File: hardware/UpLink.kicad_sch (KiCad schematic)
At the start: 20 parts, among them U1 SAM-M10Q-00B, U2 XIAO-ESP32-S3-SMD, U3 114993390, U4 TPS631000DRLR

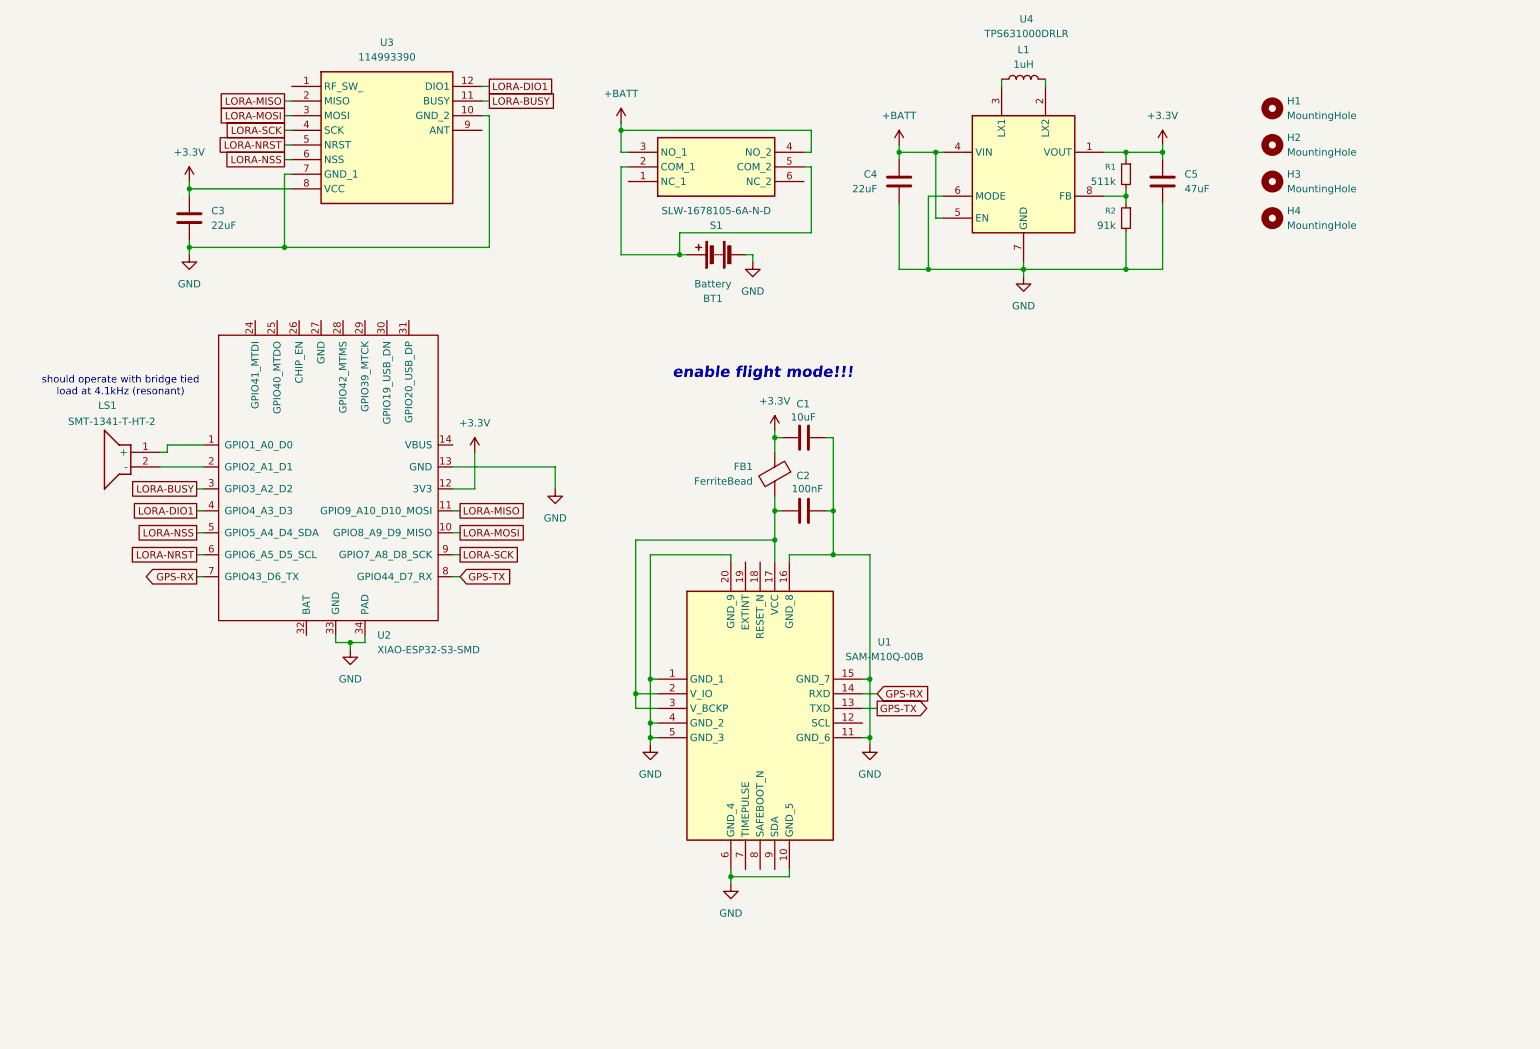
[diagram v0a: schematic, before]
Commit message: Clean up schematic
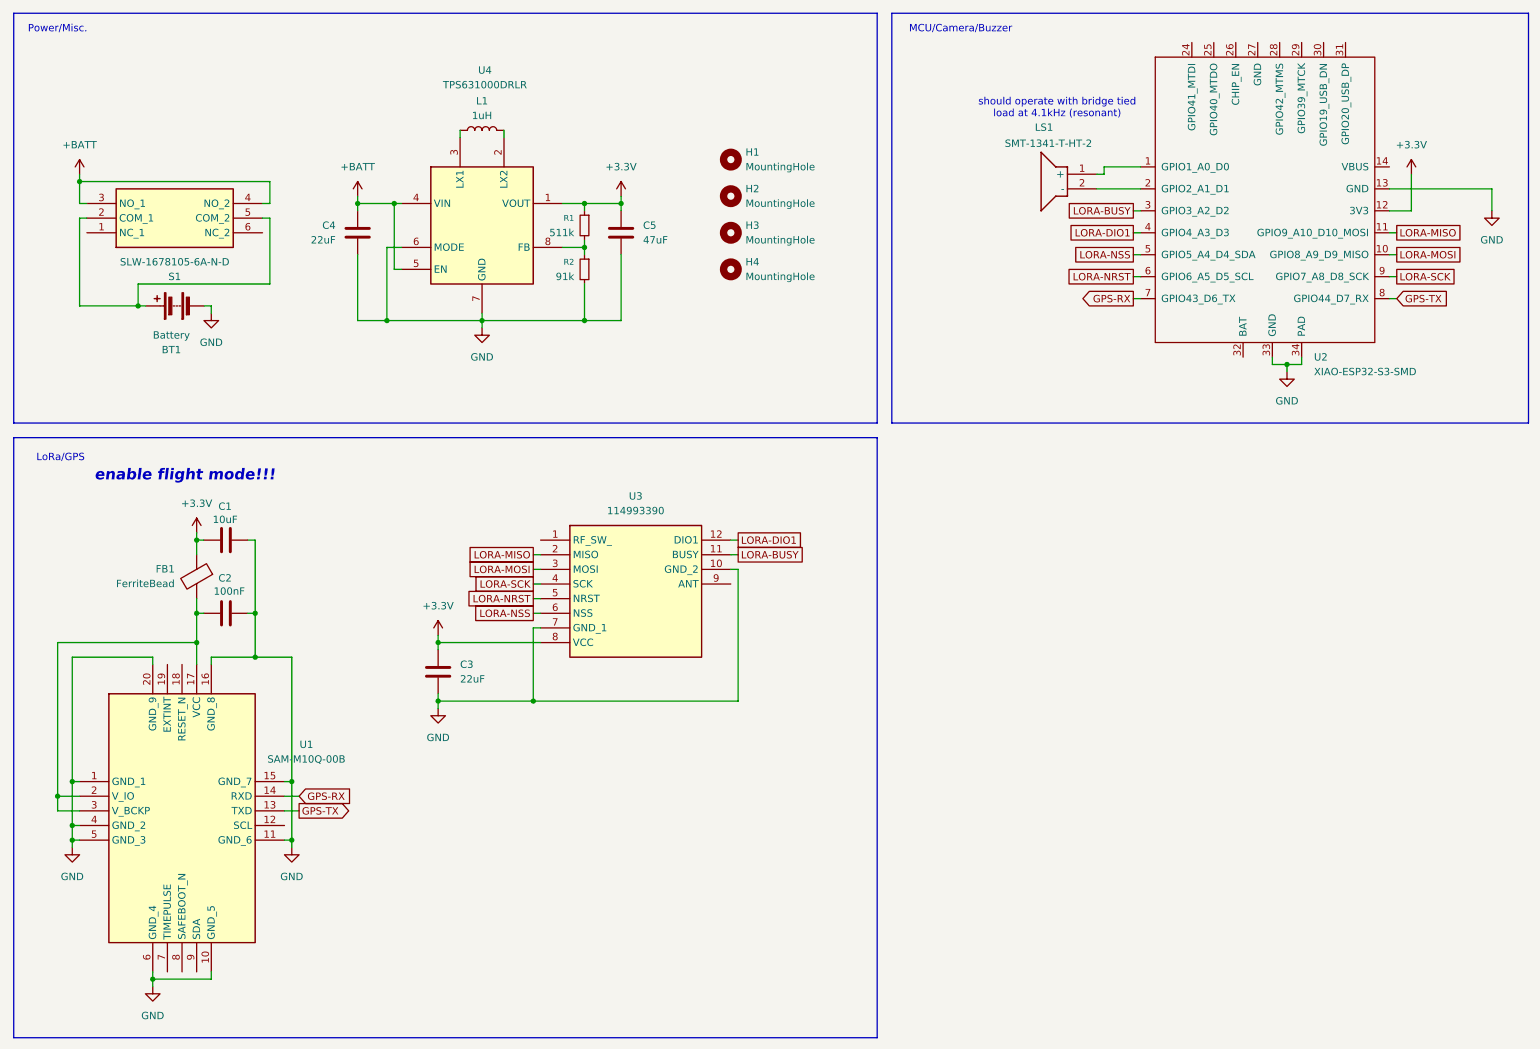
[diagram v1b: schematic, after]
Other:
- note added: "LoRa/GPS"
- note added: "MCU/Camera/Buzzer"
- note added: "Power/Misc."
- moved on the sheet: BT1, C1, C2, C3, C4, C5, FB1, H1, H2, H3, H4, L1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

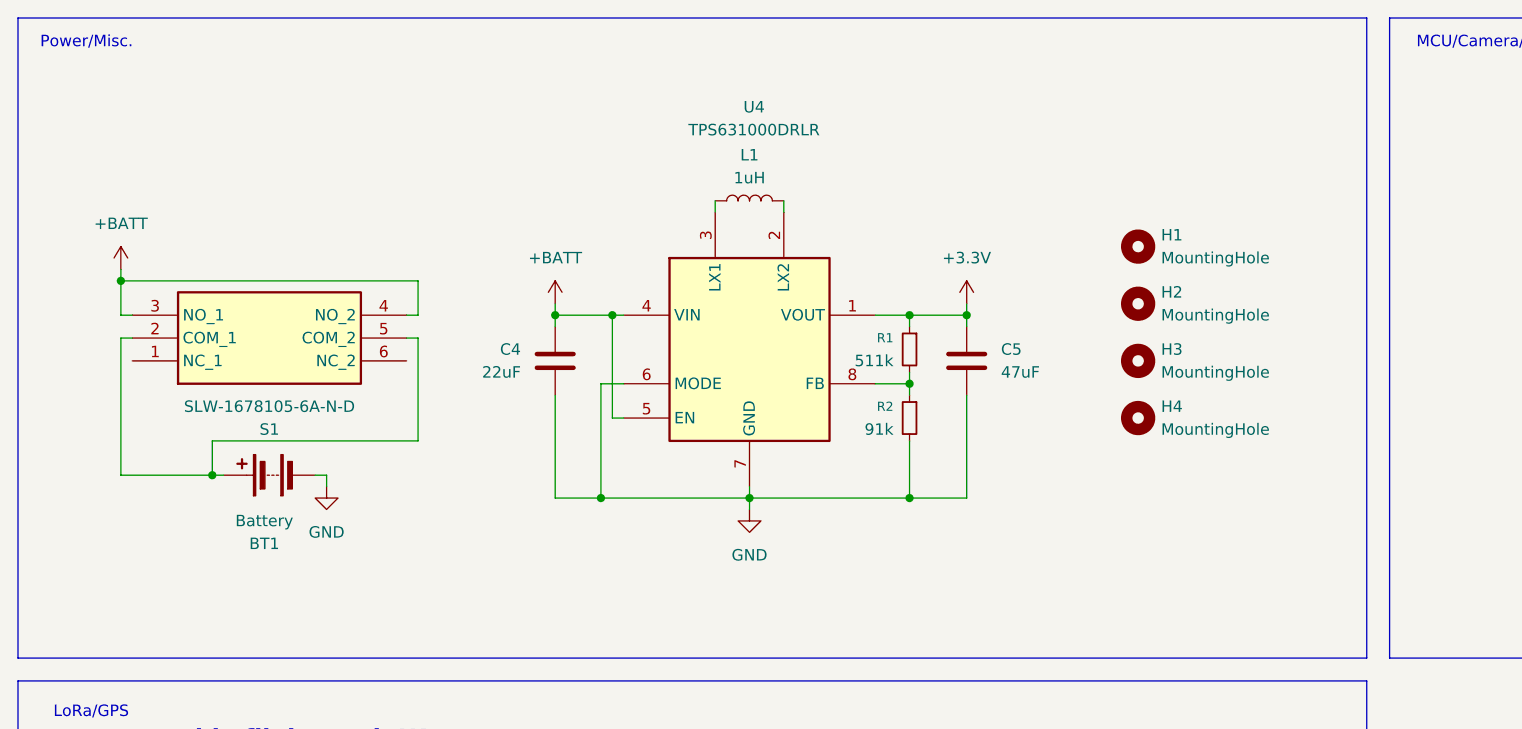
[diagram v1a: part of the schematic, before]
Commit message: Add TPS22917DBV for high side switching of payload, redesign layout for thinner board at cost of slight GPS performance hits
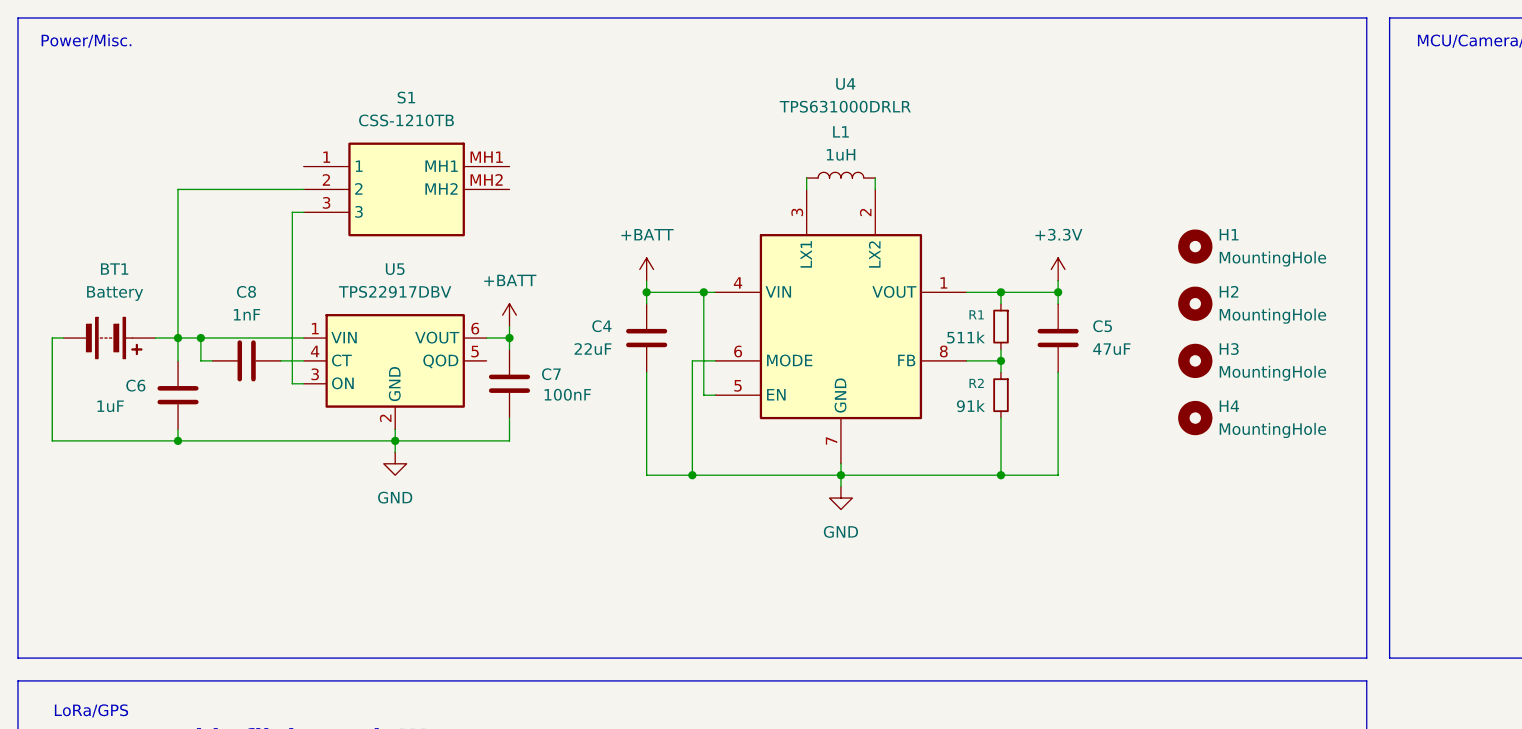
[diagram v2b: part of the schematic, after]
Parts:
- removed S1: SLW-1678105-6A-N-D, SLW-1678105-6A-N-D:SLW16781056AND, symbol SLW-1678105-6A-N-D:SLW-1678105-6A-N-D
- added C6: 1uF, Capacitor_SMD:C_0603_1608Metric, symbol Device:C
- added C7: 100nF, Capacitor_SMD:C_0603_1608Metric, symbol Device:C
- added C8: 1nF, symbol Device:C
- added S1: CSS-1210TB, CSS1210TB, symbol CSS-1210TB:CSS-1210TB
- added U5: TPS22917DBV, Package_TO_SOT_SMD:SOT-23-6, symbol Power_Management:TPS22917DBV
- BT1: Mouser Part (none) -> 12BHC431A-GR
- H1, H2, H3, H4: footprint MountingHole:MountingHole_2.2mm_M2 -> MountingHole:MountingHole_2.2mm_M2_Pad
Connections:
- net +BATT: now also C7.2, U5.6 (VOUT)
- net GND: now also C6.1, C7.1, U5.2 (GND)
- net at BT1.1 (+): now also C6.2, C8.1, S1.2, U5.1 (VIN)
- new net: C8.2, U5.4 (CT)
- new net: S1.3, U5.3 (ON)
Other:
- moved on the sheet: BT1, C4, C5, H1, H2, H3, H4, L1, R1, R2, U4

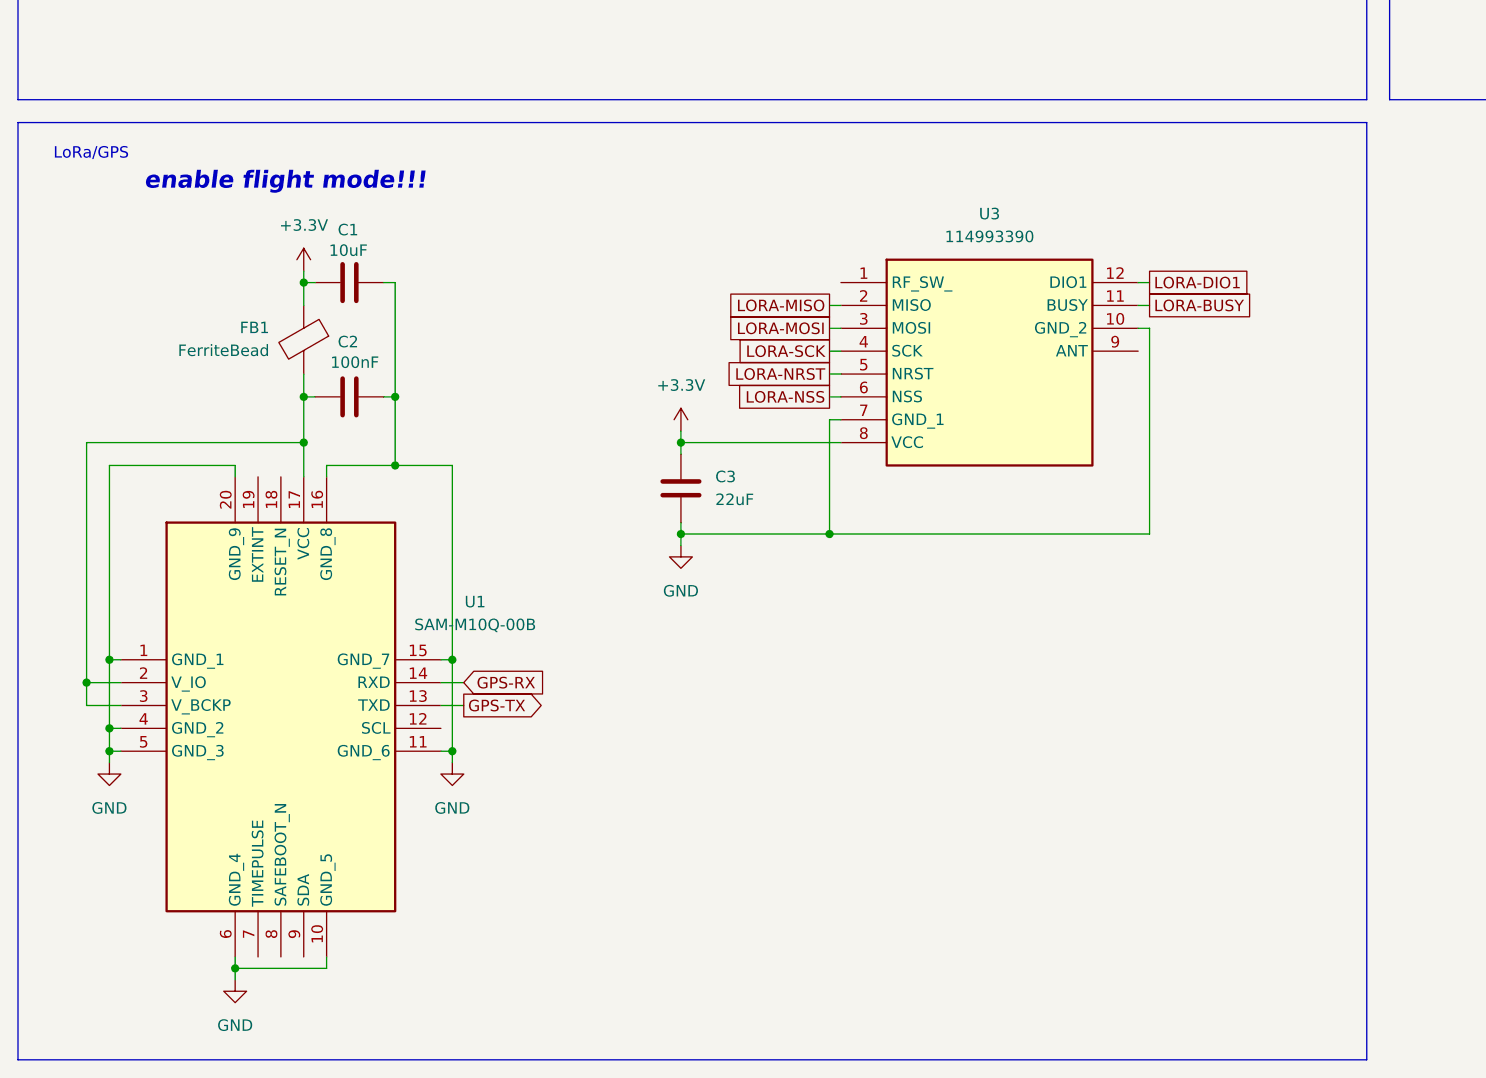
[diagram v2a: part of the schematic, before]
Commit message: Add notes to schematic
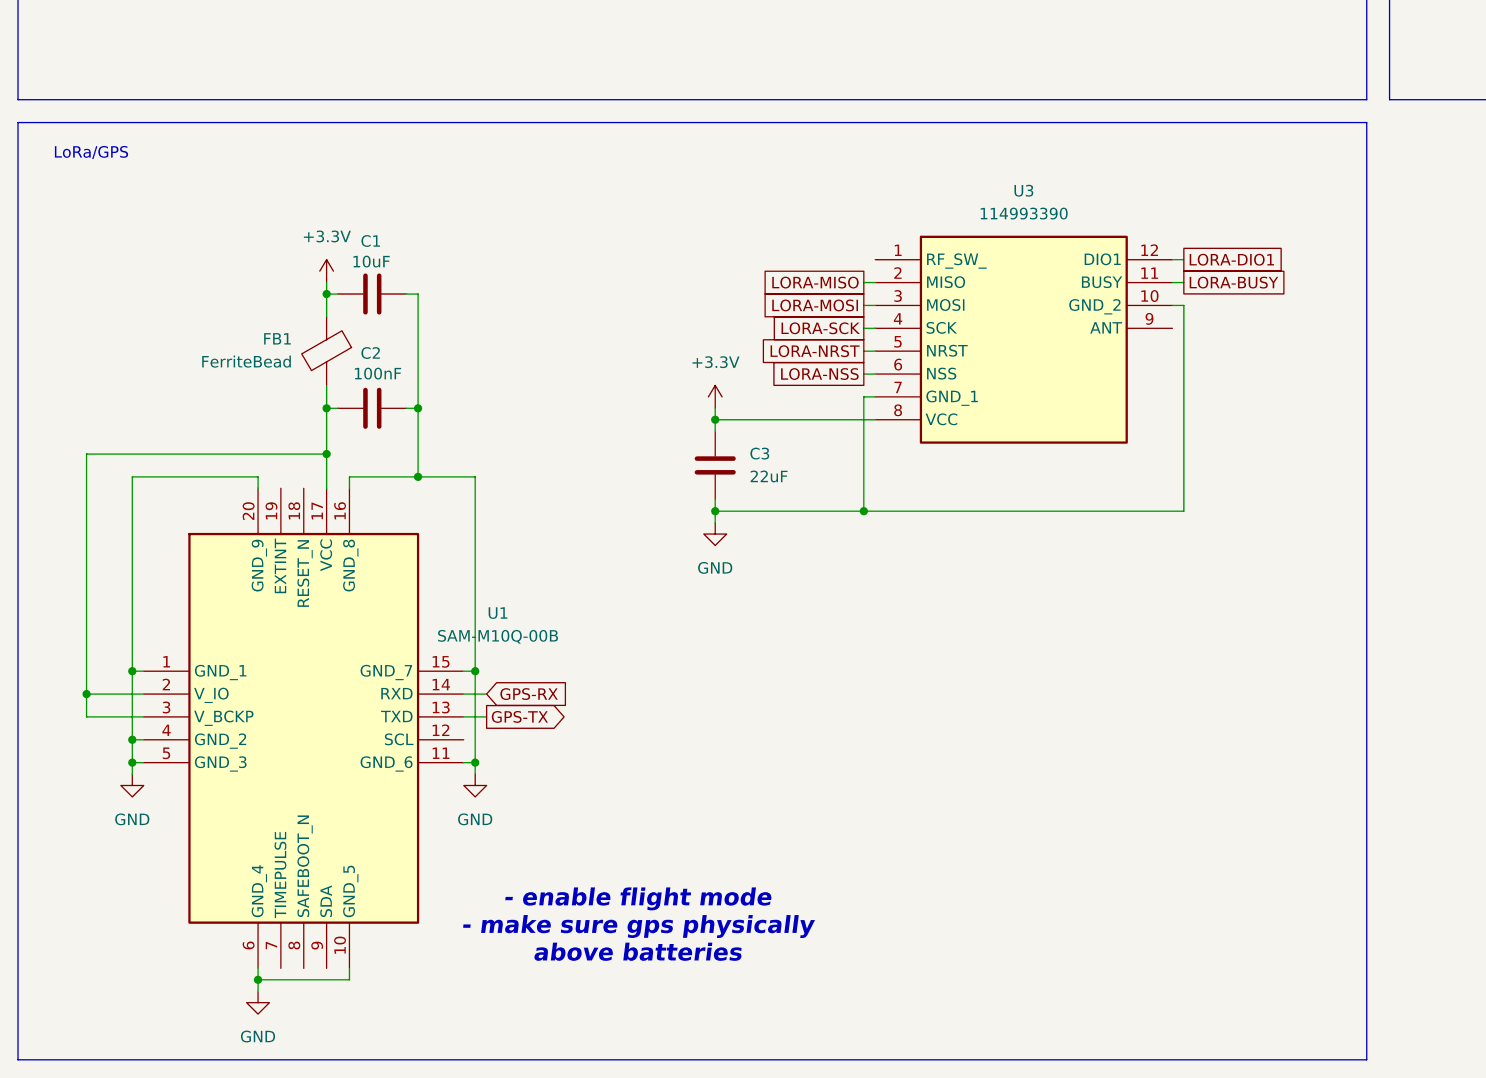
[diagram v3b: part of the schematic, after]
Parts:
- L1: Mouser Part (none) -> 81-DFE252012F-1R0MP2
- R1: Mouser Part (none) -> 603-RT0603FRE07511KL
- R2: Mouser Part (none) -> 603-AC0603JR-0791KL
- U4: Mouser Part (none) -> 595-TPS631000DRLR
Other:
- note added: "- enable flight mode - make sure gps physically above batteries"
- note removed: "enable flight mode!!!"
- moved on the sheet: C1, C2, C3, FB1, U1, U3

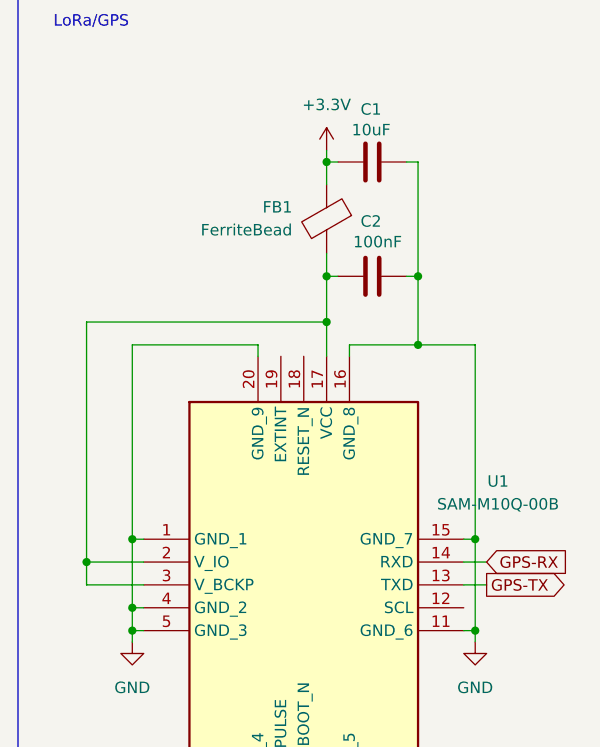
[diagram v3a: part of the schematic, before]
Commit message: Redo layout and routing, space traces apart
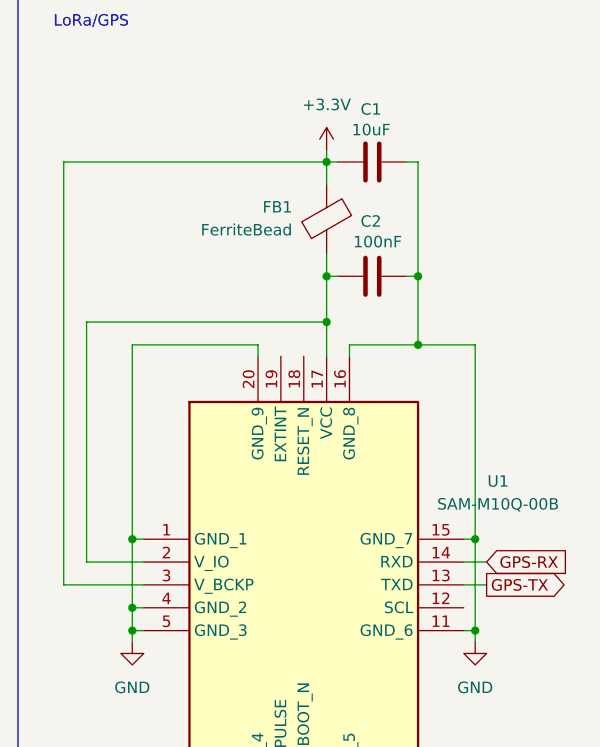
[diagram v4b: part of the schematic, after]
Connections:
- net +3.3V: now also U1.3 (V_BCKP)
- net at C2.1, FB1.2, U1.17 (VCC)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: no longer U1.3 (V_BCKP)
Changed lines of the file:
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@@
-	)
-	(junction
-		(at 26.67 154.94)
-		(diameter 0)
-		(color 0 0 0 0)
 	)
 	(junction
@@
 	(wire
 		(pts
-			(xy 26.67 154.94) (xy 26.67 157.48)
-		)
-		(stroke
-			(width 0)
-			(type default)
-		)
-	)
-	(wire
-		(pts
 			(xy 208.28 44.45) (xy 214.63 44.45)
 		)
@@
 	(wire
 		(pts
+			(xy 33.02 157.48) (xy 24.13 157.48)
+		)
+		(stroke
+			(width 0)
+			(type default)
+		)
+	)
+	(wire
+		(pts
 			(xy 93.98 55.88) (xy 93.98 68.58)
 		)
@@
 	(wire
 		(pts
-			(xy 26.67 157.48) (xy 33.02 157.48)
-		)
-		(stroke
-			(width 0)
-			(type default)
-		)
-	)
-	(wire
-		(pts
 			(xy 93.98 68.58) (xy 110.49 68.58)
 		)
@@
 	(wire
 		(pts
+			(xy 24.13 110.49) (xy 53.34 110.49)
+		)
+		(stroke
+			(width 0)
+			(type default)
+		)
+	)
+	(wire
+		(pts
 			(xy 147.32 109.22) (xy 148.59 109.22)
 		)
@@
 		)
 		(stroke
+			(width 0)
+			(type default)
+		)
+	)
+	(wire
+		(pts
+			(xy 24.13 157.48) (xy 24.13 110.49)
+		)
+		(stroke
